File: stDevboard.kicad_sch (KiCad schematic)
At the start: 21 parts, among them IC1 MPM3610GQV-Z, J1 battery, J11 USB_C_Receptacle_USB2.0_16P, J2 USB_C_Receptacle_USB2.0_16P, J3 Conn_02x03_Top_Bottom

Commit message: worked mainly on pcb
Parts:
- J3: footprint Connector_PinHeader_2.54mm:PinHeader_2x02_P2.54mm_Vertical -> Connector_PinHeader_2.54mm:PinHeader_2x03_P2.54mm_Vertical
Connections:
- net +3.3V: now also J3.2 (Pin_2); no longer J3.6 (Pin_6)
- net GND: now also J3.1 (Pin_1); no longer J3.3 (Pin_3)
- net mpu_rx_external: now also J3.6 (Pin_6); no longer J3.2 (Pin_2)
- net mpu_tx_external: now also J3.4 (Pin_4); no longer J3.1 (Pin_1)
- net ppu_tx_external: now also J3.3 (Pin_3); no longer J3.4 (Pin_4)
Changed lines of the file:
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@@
 	(wire
 		(pts
+			(xy 162.56 106.68) (xy 162.56 107.95)
+		)
+		(stroke
+			(width 0)
+			(type default)
+		)
+	)
+	(wire
+		(pts
 			(xy 29.21 26.67) (xy 29.21 25.4)
 		)
@@
 	(wire
 		(pts
-			(xy 201.93 111.76) (xy 180.34 111.76)
+			(xy 29.21 21.59) (xy 29.21 22.86)
 		)
 		(stroke
@@
 	(wire
 		(pts
-			(xy 29.21 21.59) (xy 29.21 22.86)
+			(xy 165.1 109.22) (xy 167.64 109.22)
 		)
 		(stroke
@@
 	(wire
 		(pts
+			(xy 167.64 106.68) (xy 162.56 106.68)
+		)
+		(stroke
+			(width 0)
+			(type default)
+		)
+	)
+	(wire
+		(pts
 			(xy 156.21 46.99) (xy 157.48 46.99)
 		)
@@
 	(wire
 		(pts
-			(xy 180.34 109.22) (xy 181.61 109.22)
+			(xy 180.34 106.68) (xy 181.61 106.68)
 		)
 		(stroke
@@
 	(wire
 		(pts
-			(xy 166.37 109.22) (xy 167.64 109.22)
-		)
-		(stroke
-			(width 0)
-			(type default)
-		)
-	)
-	(wire
-		(pts
 			(xy 46.99 53.34) (xy 48.26 53.34)
 		)
@@
 	(wire
 		(pts
-			(xy 166.37 113.03) (xy 166.37 111.76)
-		)
-		(stroke
-			(width 0)
-			(type default)
-		)
-	)
-	(wire
-		(pts
 			(xy 115.57 39.37) (xy 115.57 40.64)
 		)
@@
 	(wire
 		(pts
-			(xy 166.37 111.76) (xy 167.64 111.76)
+			(xy 46.99 55.88) (xy 48.26 55.88)
 		)
 		(stroke
@@
 	(wire
 		(pts
-			(xy 46.99 55.88) (xy 48.26 55.88)
+			(xy 121.92 59.69) (xy 123.19 59.69)
 		)
 		(stroke
@@
 	(wire
 		(pts
-			(xy 121.92 59.69) (xy 123.19 59.69)
+			(xy 156.21 54.61) (xy 157.48 54.61)
 		)
 		(stroke
@@
 	(wire
 		(pts
-			(xy 156.21 54.61) (xy 157.48 54.61)
+			(xy 29.21 22.86) (xy 27.94 22.86)
 		)
 		(stroke
@@
 	(wire
 		(pts
-			(xy 29.21 22.86) (xy 27.94 22.86)
+			(xy 48.26 110.49) (xy 48.26 113.03)
 		)
 		(stroke
@@
 	(wire
 		(pts
-			(xy 48.26 110.49) (xy 48.26 113.03)
+			(xy 24.13 78.74) (xy 24.13 80.01)
 		)
 		(stroke
@@
 	(wire
 		(pts
-			(xy 24.13 78.74) (xy 24.13 80.01)
+			(xy 180.34 109.22) (xy 181.61 109.22)
 		)
 		(stroke
@@
 	(wire
 		(pts
+			(xy 180.34 111.76) (xy 181.61 111.76)
+		)
+		(stroke
+			(width 0)
+			(type default)
+		)
+	)
+	(wire
+		(pts
 			(xy 173.99 54.61) (xy 173.99 53.34)
 		)
@@
 	(wire
 		(pts
-			(xy 201.93 110.49) (xy 201.93 111.76)
+			(xy 31.75 20.32) (xy 31.75 22.86)
 		)
 		(stroke
@@
 	(wire
 		(pts
-			(xy 31.75 20.32) (xy 31.75 22.86)
+			(xy 279.4 157.48) (xy 278.13 157.48)
 		)
 		(stroke
@@
 	(wire
 		(pts
-			(xy 279.4 157.48) (xy 278.13 157.48)
+			(xy 166.37 111.76) (xy 167.64 111.76)
 		)
 		(stroke
@@
 	(wire
 		(pts
-			(xy 180.34 106.68) (xy 181.61 106.68)
-		)
-		(stroke
-			(width 0)
-			(type default)
-		)
-	)
-	(wire
-		(pts
 			(xy 46.99 48.26) (xy 48.26 48.26)
 		)
@@
 	(wire
 		(pts
-			(xy 166.37 106.68) (xy 167.64 106.68)
-		)
-		(stroke
-			(width 0)
-			(type default)
-		)
-	)
-	(wire
-		(pts
 			(xy 35.56 27.94) (xy 31.75 27.94)
 		)
@@
 	(global_label "mpu_rx_external"
 		(shape output)
-		(at 166.37 109.22 180)
+		(at 181.61 111.76 0)
 		(fields_autoplaced yes)
 		(effects
@@
 				(size 1.27 1.27)
 			)
-			(justify right)
+			(justify left)
 		)
 		(property "Intersheetrefs" "${INTERSHEET_REFS}"
-			(at 147.9636 109.22 0)
+			(at 200.0164 111.76 0)
 			(effects
 				(font
 					(size 1.27 1.27)
 				)
-				(justify right)
+				(justify left)
 				(hide yes)
 			)
@@
 	(global_label "mpu_tx_external"
 		(shape input)
-		(at 166.37 106.68 180)
+		(at 181.61 106.68 0)
 		(fields_autoplaced yes)
 		(effects
@@
 				(size 1.27 1.27)
 			)
-			(justify right)
+			(justify left)
 		)
 		(property "Intersheetrefs" "${INTERSHEET_REFS}"
-			(at 148.0241 106.68 0)
+			(at 199.9559 106.68 0)
 			(effects
 				(font
 					(size 1.27 1.27)
 				)
-				(justify right)
+				(justify left)
 				(hide yes)
 			)
@@
 	(global_label "ppu_tx_external"
 		(shape input)
-		(at 181.61 106.68 0)
+		(at 166.37 111.76 180)
 		(fields_autoplaced yes)
 		(effects
@@
 				(size 1.27 1.27)
 			)
-			(justify left)
+			(justify right)
 		)
 		(property "Intersheetrefs" "${INTERSHEET_REFS}"
-			(at 199.4116 106.68 0)
+			(at 148.5684 111.76 0)
 			(effects
 				(font
 					(size 1.27 1.27)
 				)
-				(justify left)
+				(justify right)
 				(hide yes)
 			)
@@
 		(on_board yes)
 		(dnp no)
-		(fields_autoplaced yes)
 		(property "Reference" "J3"
 			(at 173.99 100.33 0)
@@
 		)
 		(property "Value" "Conn_02x03_Top_Bottom"
-			(at 173.99 102.87 0)
+			(at 175.26 102.87 0)
 			(effects
 				(font
@@
 			)
 		)
-		(property "Footprint" "Connector_PinHeader_2.54mm:PinHeader_2x02_P2.54mm_Vertical"
+		(property "Footprint" "Connector_PinHeader_2.54mm:PinHeader_2x03_P2.54mm_Vertical"
 			(at 172.72 109.22 0)
 			(effects
@@
 	(symbol
 		(lib_id "power:GND")
-		(at 166.37 113.03 0)
+		(at 162.56 107.95 0)
 		(unit 1)
 		(exclude_from_sim no)
@@
 		(fields_autoplaced yes)
 		(property "Reference" "#PWR084"
-			(at 166.37 119.38 0)
+			(at 162.56 114.3 0)
 			(effects
 				(font
@@
 		)
 		(property "Value" "GND"
-			(at 166.37 118.11 0)
+			(at 162.56 113.03 0)
 			(effects
 				(font
@@
 		)
 		(property "Footprint" ""
-			(at 166.37 113.03 0)
+			(at 162.56 107.95 0)
 			(effects
 				(font
@@
 		)
 		(property "Datasheet" ""
-			(at 166.37 113.03 0)
+			(at 162.56 107.95 0)
 			(effects
 				(font
@@
 		)
 		(property "Description" "Power symbol creates a global label with name \"GND\" , ground"
-			(at 166.37 113.03 0)
+			(at 162.56 107.95 0)
 			(effects
 				(font
@@
 	(symbol
 		(lib_id "power:+3.3V")
-		(at 201.93 110.49 0)
+		(at 165.1 109.22 0)
 		(unit 1)
 		(exclude_from_sim no)
@@
 		(fields_autoplaced yes)
 		(property "Reference" "#PWR095"
-			(at 201.93 114.3 0)
+			(at 165.1 113.03 0)
 			(effects
 				(font
@@
 		)
 		(property "Value" "+3.3V"
-			(at 201.93 105.41 0)
+			(at 165.1 104.14 0)
 			(effects
 				(font
@@
 		)
 		(property "Footprint" ""
-			(at 201.93 110.49 0)
+			(at 165.1 109.22 0)
 			(effects
 				(font
@@
 		)
 		(property "Datasheet" ""
-			(at 201.93 110.49 0)
+			(at 165.1 109.22 0)
 			(effects
 				(font
@@
 		)
 		(property "Description" "Power symbol creates a global label with name \"+3.3V\""
-			(at 201.93 110.49 0)
+			(at 165.1 109.22 0)
 			(effects
 				(font

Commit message: worked on adding mosfet stuff, last of the major signal traces routed
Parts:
- J1: footprint Connector_PinHeader_2.54mm:PinHeader_1x02_P2.54mm_Vertical -> TerminalBlock:TerminalBlock_Xinya_XY308-2.54-2P_1x02_P2.54mm_Horizontal
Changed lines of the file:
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@@
 			)
 		)
-		(property "Footprint" "Connector_PinHeader_2.54mm:PinHeader_1x02_P2.54mm_Vertical"
+		(property "Footprint" "TerminalBlock:TerminalBlock_Xinya_XY308-2.54-2P_1x02_P2.54mm_Horizontal"
 			(at 22.86 25.4 0)
 			(effects

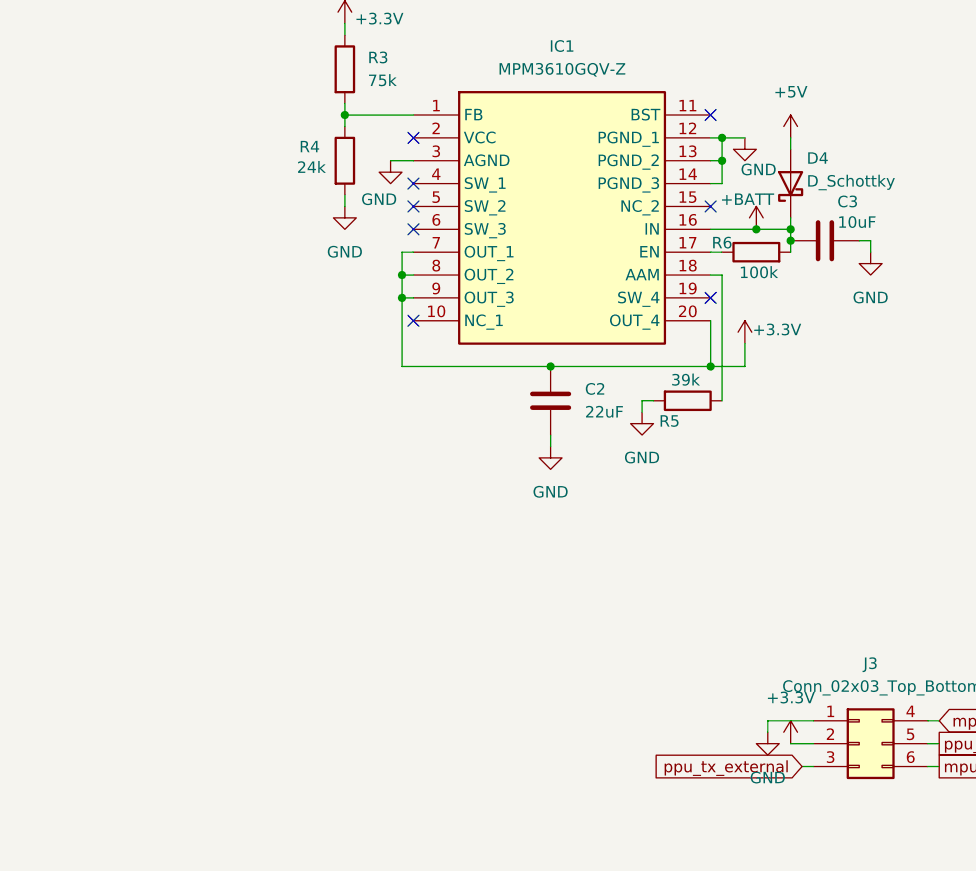
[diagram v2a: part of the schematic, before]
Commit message: added in the flash chip and micro sd card, rerouted some stuff, looking real nice rn - still need to finish rf, pyros, and add in the piezo
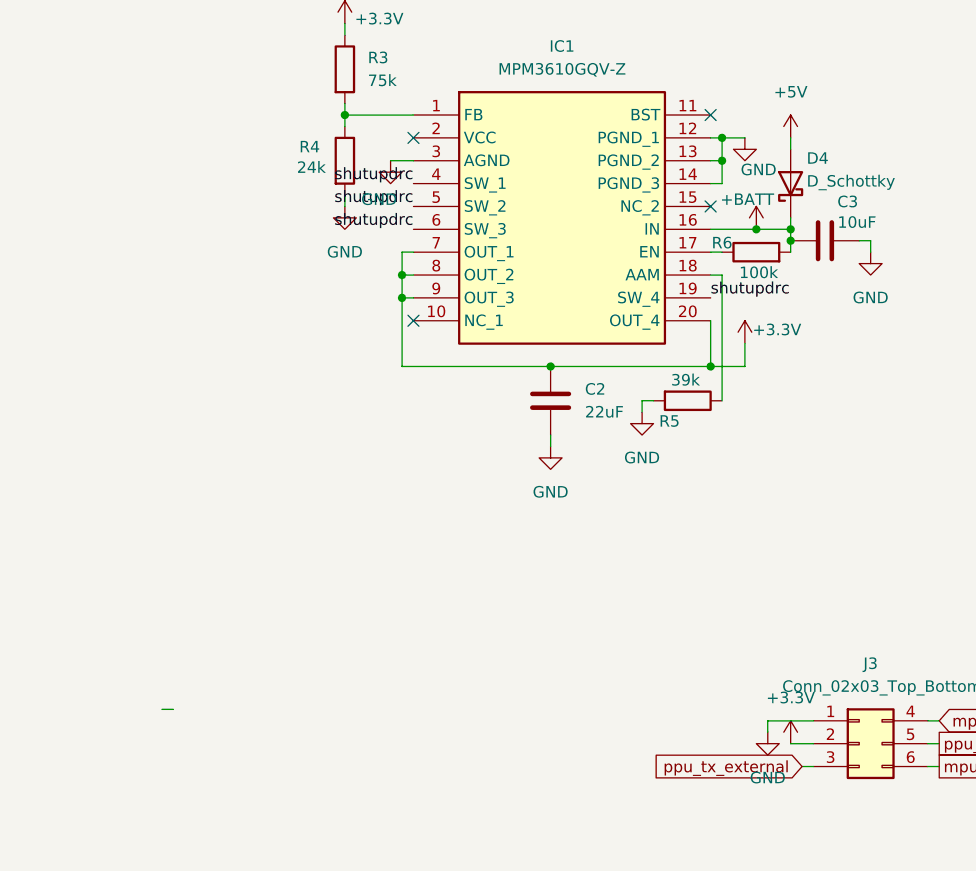
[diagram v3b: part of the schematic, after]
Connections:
- net shutupdrc: now reaches IC1.19 (SW_4)
- net shutupdrc: now also IC1.4 (SW_1), IC1.5 (SW_2), IC1.6 (SW_3)
- no-connect marks 12 -> 8
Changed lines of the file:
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@@
-	)
-	(no_connect
-		(at 156.21 59.69)
 	)
 	(no_connect
@@
 	)
 	(no_connect
-		(at 123.19 46.99)
-	)
-	(no_connect
-		(at 123.19 52.07)
-	)
-	(no_connect
 		(at 123.19 41.91)
 	)
@@
 		(at 156.21 39.37)
 	)
-	(no_connect
-		(at 123.19 49.53)
-	)
 	(wire
 		(pts
@@
 	(wire
 		(pts
+			(xy 95.25 105.41) (xy 96.52 105.41)
+		)
+		(stroke
+			(width 0)
+			(type default)
+		)
+	)
+	(wire
+		(pts
 			(xy 156.21 54.61) (xy 157.48 54.61)
 		)
@@
 		)
 	)
+	(label "shutupdrc"
+		(at 123.19 46.99 180)
+		(effects
+			(font
+				(size 1.27 1.27)
+			)
+			(justify right bottom)
+		)
+	)
+	(label "shutupdrc"
+		(at 156.21 59.69 0)
+		(effects
+			(font
+				(size 1.27 1.27)
+			)
+			(justify left bottom)
+		)
+	)
+	(label "shutupdrc"
+		(at 123.19 49.53 180)
+		(effects
+			(font
+				(size 1.27 1.27)
+			)
+			(justify right bottom)
+		)
+	)
+	(label "shutupdrc"
+		(at 123.19 52.07 180)
+		(effects
+			(font
+				(size 1.27 1.27)
+			)
+			(justify right bottom)
+		)
+	)

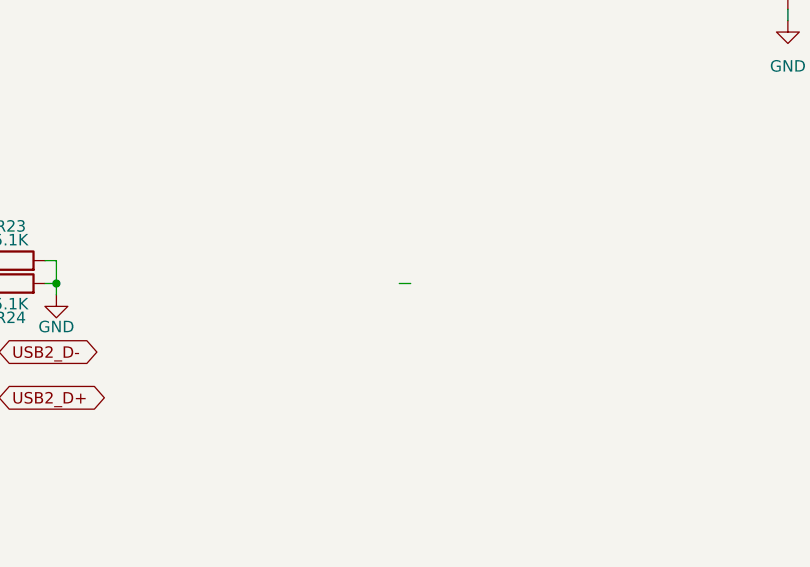
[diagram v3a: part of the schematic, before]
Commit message: added piezo buzzer, rf hopefully finished! just need to send to mpk for check now
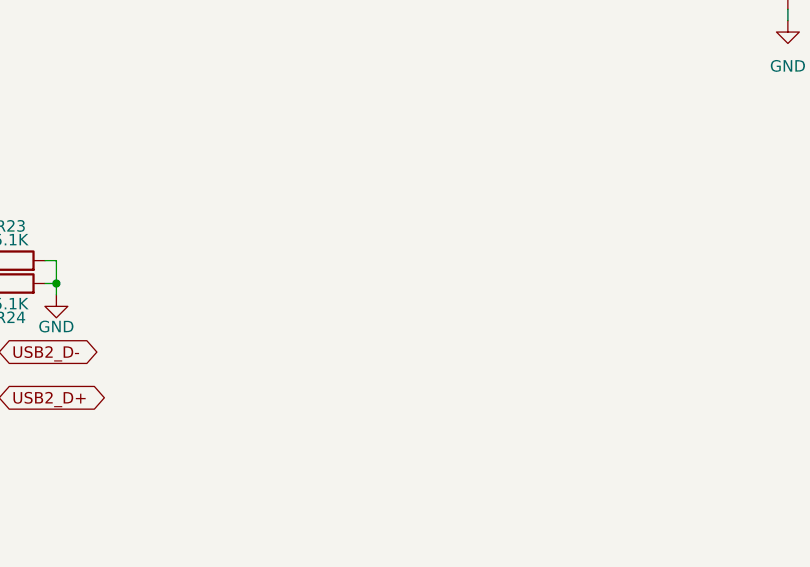
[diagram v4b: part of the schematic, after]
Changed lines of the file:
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@@
-	(wire
-		(pts
-			(xy 95.25 105.41) (xy 96.52 105.41)
-		)
-		(stroke
-			(width 0)
-			(type default)
-		)
-	)
 	(wire
 		(pts

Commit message: idk what I did but it wasn't saved
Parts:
- R3, R4, R5: footprint Resistor_SMD:R_0201_0603Metric -> Resistor_SMD:R_0402_1005Metric
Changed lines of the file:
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@@
 			)
 		)
-		(property "Footprint" "Resistor_SMD:R_0201_0603Metric"
+		(property "Footprint" "Resistor_SMD:R_0402_1005Metric"
 			(at 113.792 34.29 90)
 			(effects
@@
 			)
 		)
-		(property "Footprint" "Resistor_SMD:R_0201_0603Metric"
+		(property "Footprint" "Resistor_SMD:R_0402_1005Metric"
 			(at 153.67 69.342 90)
 			(effects
@@
 			)
 		)
-		(property "Footprint" "Resistor_SMD:R_0201_0603Metric"
+		(property "Footprint" "Resistor_SMD:R_0402_1005Metric"
 			(at 113.792 44.45 90)
 			(effects
